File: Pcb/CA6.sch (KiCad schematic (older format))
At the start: 185 parts, among them J1 MICRO_USB, J2 BAT_CON, J3 MODULE_0, J4 MODULE_2, J5 MODULE_1, J6 AUX, J8 MODULE_3, P1 JTAG, P2 Connection_Card, P3 ESP-Programming-FTDI, Q1 BSS138P, Q10 BSS138P, Q11 BSS138P, Q12 BSS138P, Q13 BSS138P, Q14 BSS138P, Q15 BSS138P, Q16 BSS138P, Q2 BSS138P, Q3 BSS138P, Q4 BSS138P, Q5 BSS138P, Q6 BSS138P, Q7 BSS138P, Q8 BSS138P, Q9 BSS138P, SW1 ERASE, SW2 USB/BATTERY, SW3 RESET, SW4 BUTTON_0, U1 74LS244, U12 VREG_33, U16 ATSAM3X8EA-AU_LQFP-144, U2 74LS244, U3 SN74AHC1G08, U4 ESP-12E/F, X1 HOLE, X2 HOLE, X3 HOLE, X4 HOLE, X5 HOLE, X7 CRYSTAL_4, X8 32khz

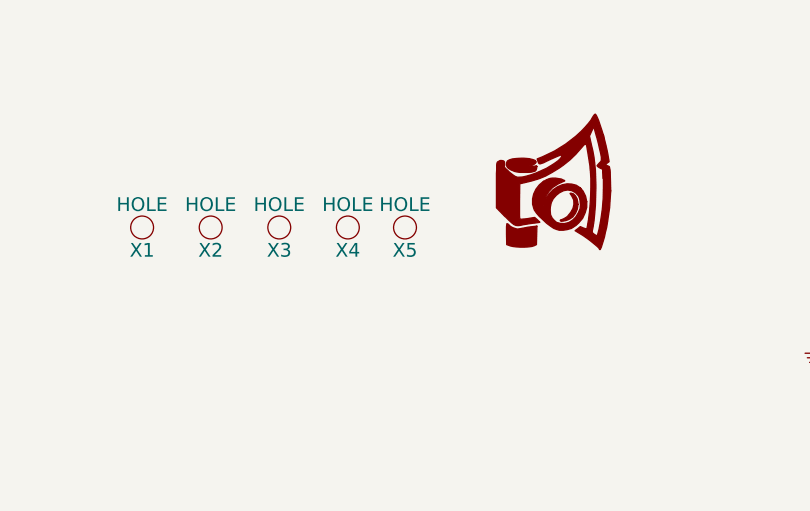
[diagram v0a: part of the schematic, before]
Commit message: Fix esp8266 layout and start routing
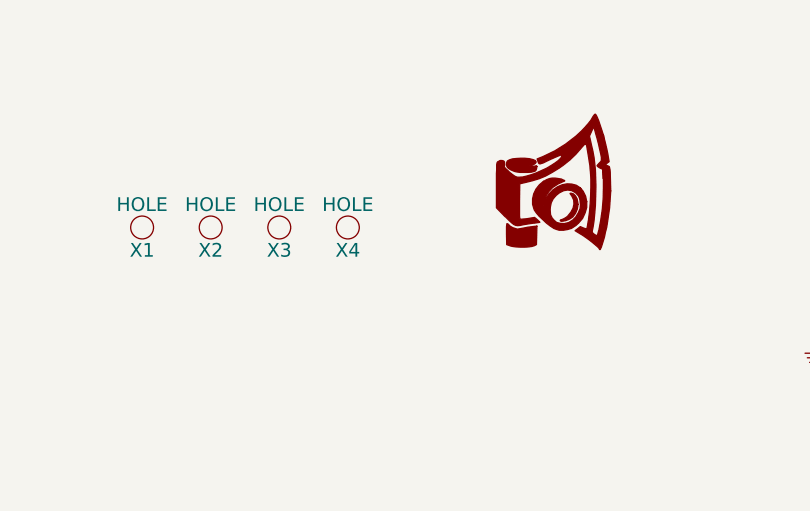
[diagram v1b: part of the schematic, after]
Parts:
- removed X5: HOLE, CA6:HOLE_3.0mm, symbol HOLE
- U4: footprint CA6:ESP-12E-F-no-bottom-pads -> CA6:ESP-12E-B
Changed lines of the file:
@@
 Text Label 18650 12100 2    60   ~ 0
 CC_EXT1
-$Comp
-L HOLE X5
-U 1 1 58D981BA
-P 8100 1500
-F 0 "X5" H 8100 1400 60  0000 C CNN
-F 1 "HOLE" H 8100 1600 60  0000 C CNN
-F 2 "CA6:HOLE_3.0mm" H 8100 1500 60  0001 C CNN
-F 3 "~" H 8100 1500 60  0000 C CNN
-	1    8100 1500
-	1    0    0    -1
-$EndComp
 Text Label 700  5400 0    60   ~ 0
 CAM0S
@@
 F 0 "U4" H 20400 13400 50  0000 C CNN
 F 1 "ESP-12E/F" H 20400 13600 50  0000 C CNN
-F 2 "CA6:ESP-12E-F-no-bottom-pads" H 20400 13500 50  0001 C CNN
+F 2 "CA6:ESP-12E-B" H 20400 13500 50  0001 C CNN
 F 3 "" H 20400 13500 50  0001 C CNN
 	1    20400 13500

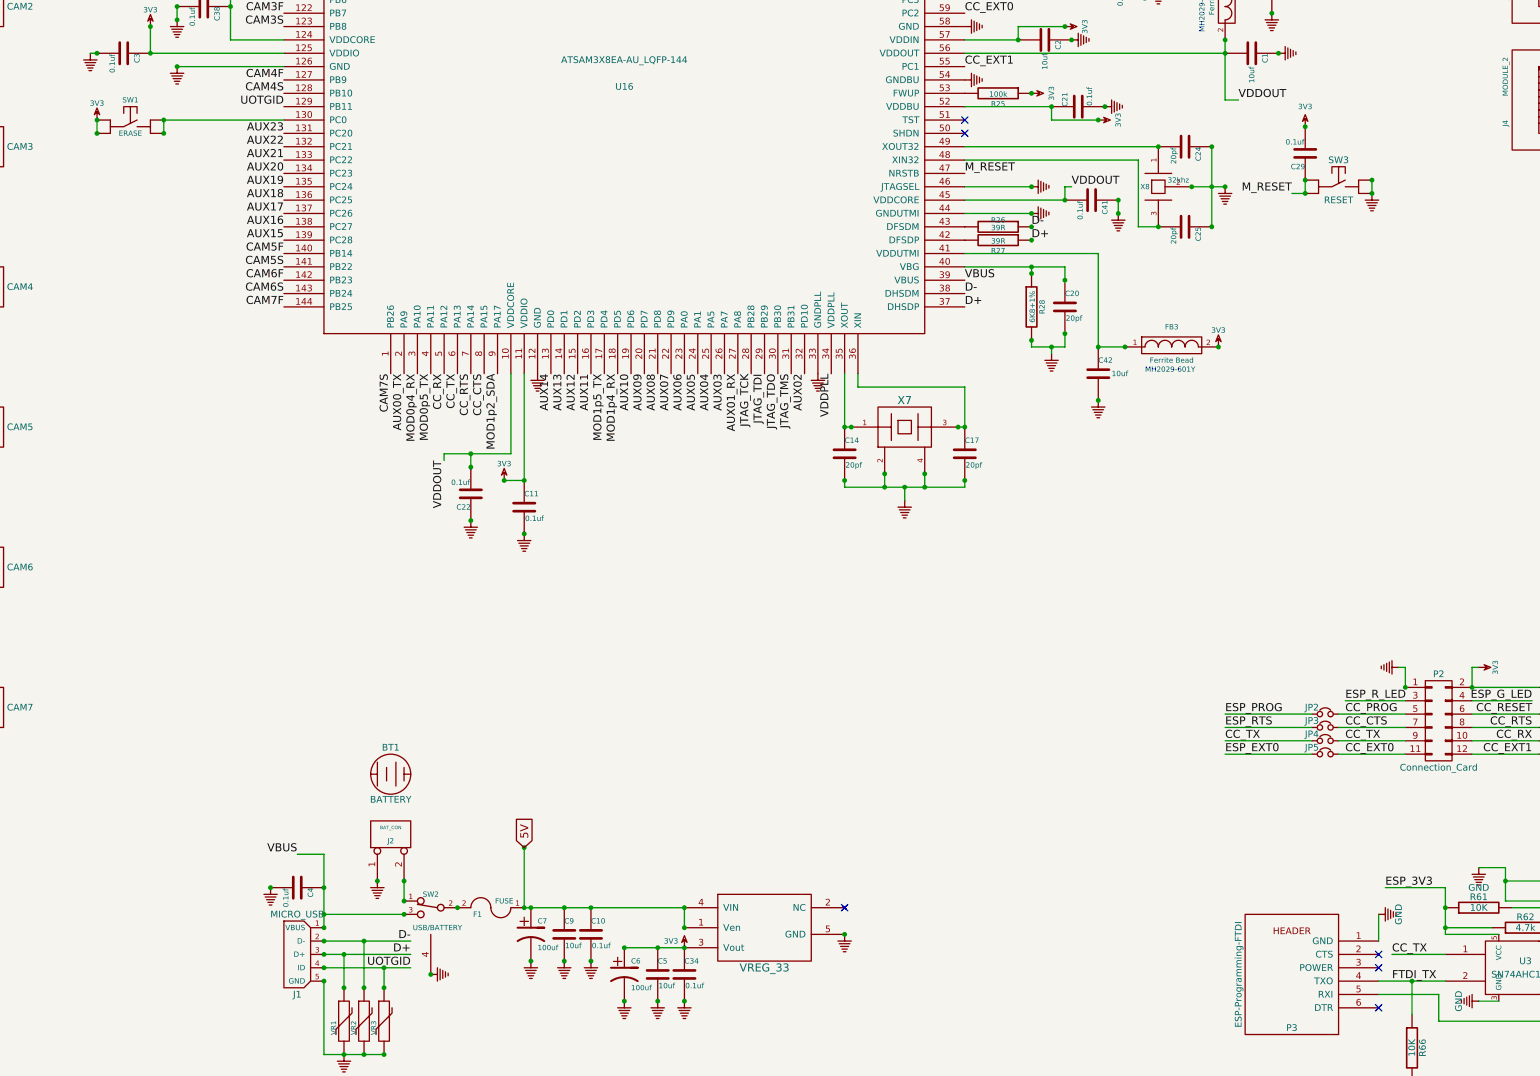
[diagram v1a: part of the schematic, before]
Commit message: Fix 3 issues pcba house found in pcb.  Update spice files.
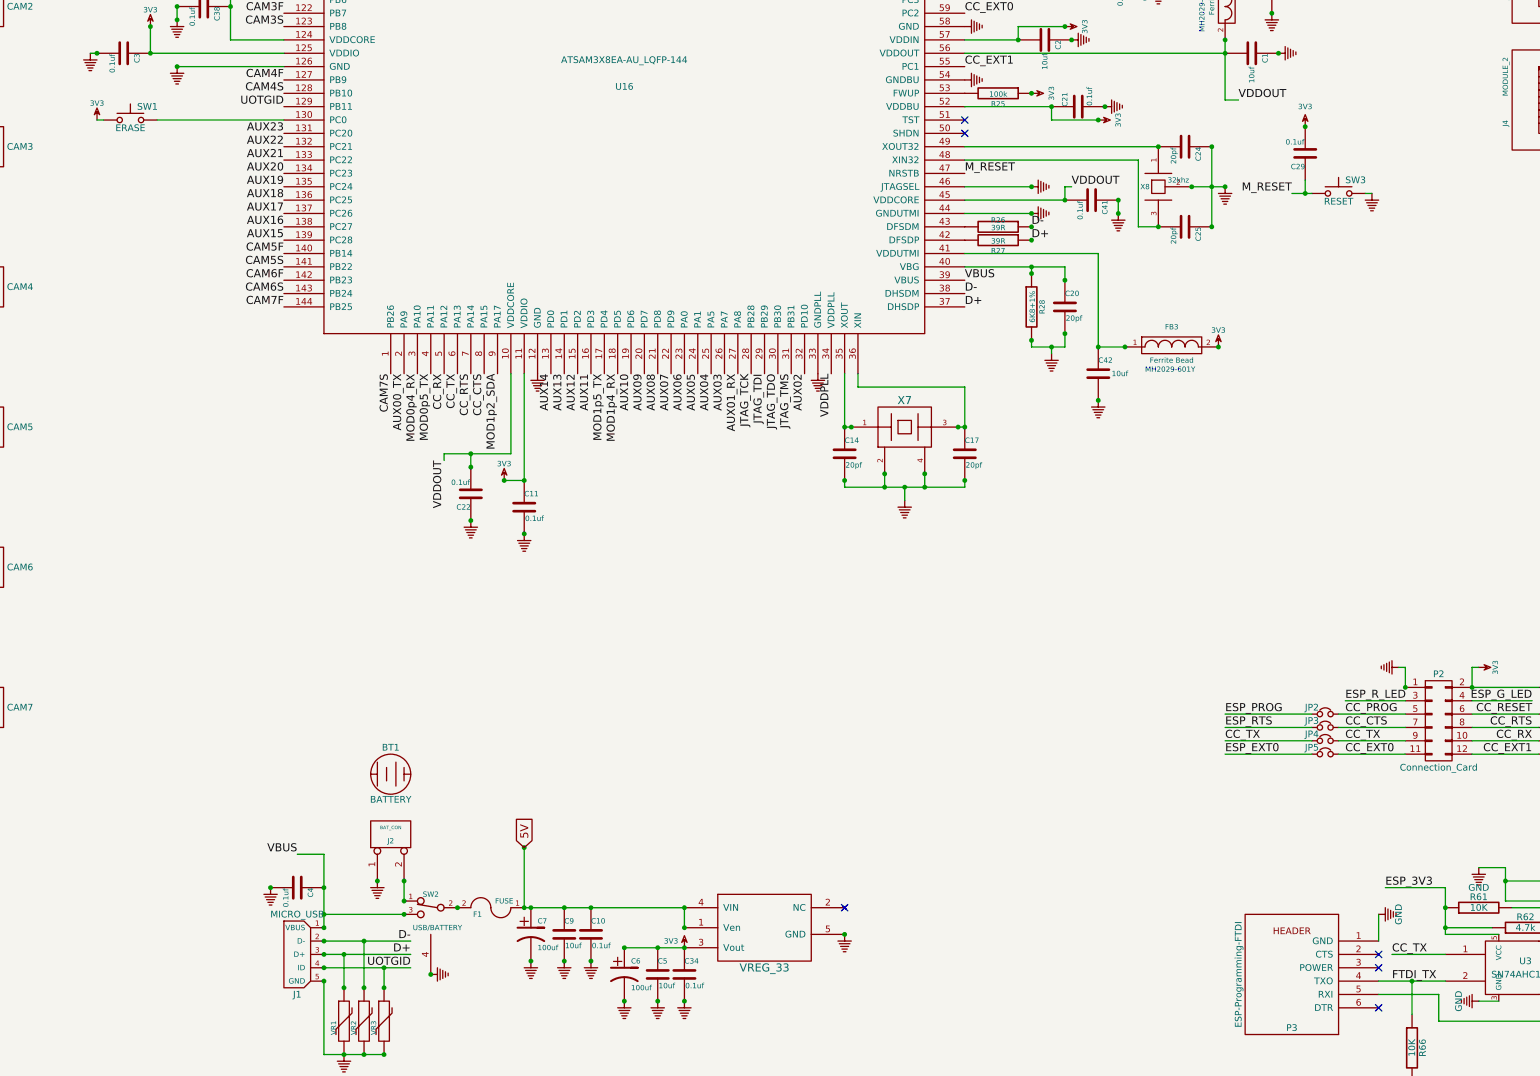
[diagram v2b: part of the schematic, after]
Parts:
- removed SW1: ERASE, Buttons_Switches_SMD:SW_SPST_PTS645, symbol SW_TACTILE
- removed SW3: RESET, Buttons_Switches_SMD:SW_SPST_PTS645, symbol SW_TACTILE
- added SW1: ERASE, Buttons_Switches_SMD:SW_SPST_PTS645, symbol SW_Push
- added SW3: RESET, Buttons_Switches_SMD:SW_SPST_PTS645, symbol SW_Push
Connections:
- net 3V3: now also SW1.1
- net GND: now also SW3.2
- net M_RESET: now also SW3.1
- net at U16.130 (PC0): now also SW1.2

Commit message: Update pcb for new switch
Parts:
- BT1: symbol BATTERY -> CA6:BATTERY
- C1, C10, C11, C12, C13, C14, C15, C16, C17, C18, C19, C2, C20, C21, C22, C24, C25, C28, C29, C3, C30, C31, C32, C33, C34, C35, C37, C38, C39, C4, C40, C41, C42, C5, C8, C9: symbol C -> CA6:C
- C23, C26, C27, C6, C7: symbol CAP_ELEC -> CA6:CAP_ELEC
- CAM0, CAM1, CAM2, CAM3, CAM4, CAM5, CAM6, CAM7: symbol JACK_STEREO -> CA6:JACK_STEREO
- D1, D2, D3, D4, D5, D6, D7, D8, D9: symbol LED2C -> CA6:LED2C
- F1: symbol FUSE -> CA6:FUSE
- FB1, FB2, FB3: symbol FILTER -> CA6:FILTER
- J1: symbol MICRO_USB -> CA6:MICRO_USB
- J2: symbol CONNECTOR_2 -> CA6:CONNECTOR_2
- J3, J4, J5, J8: symbol JACK_RJ45 -> CA6:JACK_RJ45
- J6: symbol IDC_50PIN(2X25) -> CA6:IDC_50PIN(2X25)
- JP10, JP2, JP3, JP4, JP5, JP6, JP7, JP8, JP9: symbol Jumper_NC_Small -> Device:Jumper_NC_Small
- LOGO1: symbol CA_Logo_150 -> CA6:CA_Logo_150
- P1: symbol JTAG_20021121-00010C4LF -> CA6:JTAG_20021121-00010C4LF
- P2: symbol CONN_02X06 -> CA6:CONN_02X06
- P3: symbol FTDI -> CA6:FTDI
- Q1, Q10, Q11, Q12, Q13, Q14, Q15, Q16, Q2, Q3, Q4, Q5, Q6, Q7, Q8, Q9: symbol BSS138P -> CA6:BSS138P
- R1, R10, R11, R12, R13, R14, R15, R16, R17, R18, R19, R2, R20, R21, R22, R23, R24, R25, R26, R27, R28, R29, R3, R30, R31, R32, R33, R34, R35, R36, R37, R38, R39, R4, R40, R41, R42, R43, R44, R45, R46, R47, R48, R49, R5, R50, R51, R52, R53, R54, R55, R56, R57, R58, R59, R6, R60, R61, R62, R63, R64, R65, R66, R7, R8, R9: symbol R -> CA6:R
- SW1, SW3: symbol SW_Push -> switches:SW_Push
- SW2: footprint CA6:Switch_pcbwing_right_3a_ts-13p -> Buttons_Switches_ThroughHole:SW_E-Switch_EG1224_SPDT_Angled; symbol SW_SPDT -> CA6:SW_SPDT
- SW4: symbol SW_TACTILE -> CA6:SW_TACTILE
- U1, U2: symbol 74LS244 -> CA6-rescue:74LS244
- U12: symbol VREG_LP38692 -> CA6:VREG_LP38692
- U16: symbol ATSAM3X8EA-AU_LQFP-144 -> CA6:ATSAM3X8EA-AU_LQFP-144
- U3: symbol SN74AHC1G08 -> CA6:SN74AHC1G08
- U4: symbol ESP-12E/F -> CA6-rescue:ESP-12E_F
- VR1, VR2, VR3: symbol VARISTOR -> CA6:VARISTOR
- X1, X2, X3, X4: symbol HOLE -> CA6:HOLE
- X7: symbol CRYSTAL_4 -> CA6:CRYSTAL_4
- X8: symbol CRYSTAL_3 -> CA6:CRYSTAL_3
